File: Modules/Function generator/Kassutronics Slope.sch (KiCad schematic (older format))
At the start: 128 parts, among them J1 PJ301M-12, J10 Conn_01x08_Female, J11 Conn_01x08_Male, J12 Conn_01x05_Female, J13 Conn_01x05_Male, J14 Conn_01x06_Female, J15 Conn_01x06_Male, J2 PJ301M-12, J3 PJ301M-12, J4 PJ301M-12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

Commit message: Function generator: tweaked EOC and EOR circuits
Added diodes to gate outputs to prevent negative "low" value.
Also tweaked trigger thresholds based on simulations ( EOR comparator )
Added some additional comments to the schematic
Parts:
- removed C6, C7: 47p, Capacitor_SMD:C_0805_2012Metric_Pad1.15x1.40mm_HandSolder_smallText, symbol Device:C_Small
- removed D9: 1N5817, Diode_THT:D_DO-41_SOD81_P10.16mm_Horizontal, symbol Diode:1N5817
- added D20, D9: FDLL4148, Eurocad:LL4148_sam, symbol Diode:1N4148
- R26: value 1M -> 100k
- R32: value 100k -> 470k
- U3, U5: footprint (none) -> Package_SO:SOIC-14_3.9x8.7mm_P1.27mm
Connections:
- net EOC_out: now also D9.1 (K); no longer D11.2 (A), R32.1, U2.14
- net EOR_out: now also D20.1 (K); no longer U5.7
- net EORjack: now reaches J5.3, R42.1
- new net: D11.2 (A), D9.2 (A), R32.1, U2.14
- new net: D20.2 (A), U5.7
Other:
- note added: "At rest, STATE is low, so \npreceeding schmitt trigger\nis output low.\n\nWhen a trigger pulse comes in, \nassuming OUT is low, the schmitt\ntrigger turns on. \nNow the schmitt trigger's own output\nholds the +ve input high, even when \nthe trigger pulse has ended\n"
- note added: "Comparator"
- note added: "EOC comparator:\n( Schmitt trigger )\n\n\nEOC = TRUE if OUT < 120mV"
- note added: "STATE is high during the attack.\nMeanwhile OUT is rising.\nWhen OUT goes above 7.5V, the schmitt\ntrigger flips and then state goes negative"
- note added: "Sustain_buf = the voltage set by the pot if \nthe output of the Schmitt trigger is high\n( otherwise the sustain voltage is shorted to \nthe output of the schmitt trigger : near -12V )"
- note added: "To do:\n\nConsider moving D14 to lower PCB?\nCheck diode types\nGate output levels : Should we use zener diodes to give well-defined gate levels?"
- note removed: "EOC comparator:\n\nEOC = TRUE if OUT < 120mV"
- note removed: "STATE is high during the attack"
- note removed: "Sustain_buf = the voltage set by the pot if \nthe output of the Schmitt trigger is high\n( otherwise the sustain voltage is shorted to near -12 )"
- note removed: "To do:\n\nConsider moving D14 to lower PCB?\nCheck diode types\nGate output levels : needs a diode I think! Also a LM339 might give cleaner 0V / xV gates"
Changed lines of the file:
@@
 	9250 8000 9075 8000
 Connection ~ 10100 7900
-Text Notes 10475 7475 0    50   ~ 0
-STATE is high during the attack
+Text Notes 9075 6775 0    50   ~ 0
+STATE is high during the attack.\nMeanwhile OUT is rising.\nWhen OUT goes above 7.5V, the schmitt\ntrigger flips and then state goes negative
 Text GLabel 8425 9150 0    50   Input ~ 0
 OUT
 $Comp
-L Diode:1N5817 D9
-U 1 1 6080D78A
-P 8950 9375
-F 0 "D9" V 8904 9455 50  0000 L CNN
-F 1 "1N5817" V 8995 9455 50  0000 L CNN
-F 2 "Diode_THT:D_DO-41_SOD81_P10.16mm_Horizontal" H 8950 9200 50  0001 C CNN
-F 3 "http://www.vishay.com/docs/88525/1n5817.pdf" H 8950 9375 50  0001 C CNN
-	1    8950 9375
-	0    1    1    0
-$EndComp
-$Comp
 L Device:R R22
 U 1 1 6080F23B
@@
 	0    1    1    0
 $EndComp
-$Comp
-L power:GND #PWR018
-U 1 1 6080F96E
-P 8950 9625
-F 0 "#PWR018" H 8950 9375 50  0001 C CNN
-F 1 "GND" H 8955 9452 50  0000 C CNN
-F 2 "" H 8950 9625 50  0001 C CNN
-F 3 "" H 8950 9625 50  0001 C CNN
-	1    8950 9625
-	1    0    0    -1
-$EndComp
-Wire Wire Line
-	8950 9525 8950 9625
 Wire Wire Line
 	8425 9150 8550 9150
-Wire Wire Line
-	8850 9150 8950 9150
-Wire Wire Line
-	8950 9150 8950 9225
-Wire Wire Line
-	8950 9150 9075 9150
-Connection ~ 8950 9150
 Connection ~ 9075 9150
 $Comp
@@
 P 9625 8375
 F 0 "R26" V 9525 8375 50  0000 C CNN
-F 1 "1M" V 9625 8375 50  0000 C CNN
+F 1 "100k" V 9625 8375 50  0000 C CNN
 F 2 "Eurocad:R_0805_2012Metric_Pad1.15x1.40mm_HandSolder_smallText" V 9555 8375 50  0001 C CNN
 F 3 "~" H 9625 8375 50  0001 C CNN
@@
 P 10950 8475
 F 0 "R32" V 10850 8475 50  0000 C CNN
-F 1 "100k" V 10950 8475 50  0000 C CNN
+F 1 "470k" V 10950 8475 50  0000 C CNN
 F 2 "Eurocad:R_0805_2012Metric_Pad1.15x1.40mm_HandSolder_smallText" V 10880 8475 50  0001 C CNN
 F 3 "~" H 10950 8475 50  0001 C CNN
@@
 Wire Wire Line
 	12475 8075 11925 8075
-Text Notes 10450 9650 0    50   ~ 0
-EOC comparator:\n\nEOC = TRUE if OUT < 120mV
+Text Notes 10475 9825 0    50   ~ 0
+EOC comparator:\n( Schmitt trigger )\n\n\nEOC = TRUE if OUT < 120mV
 Text Notes 13375 7525 0    50   ~ 0
 EOR comparator\n\nEOR = NOT ( STATE, EOC )
@@
 	8825 12950 8825 13275
 Connection ~ 8825 13275
-$Comp
-L Device:C_Small C6
-U 1 1 608F4EDC
-P 9650 6900
-F 0 "C6" V 9421 6900 50  0000 C CNN
-F 1 "47p" V 9512 6900 50  0000 C CNN
-F 2 "Capacitor_SMD:C_0805_2012Metric_Pad1.15x1.40mm_HandSolder_smallText" H 9650 6900 50  0001 C CNN
-F 3 "~" H 9650 6900 50  0001 C CNN
-	1    9650 6900
-	0    1    1    0
-$EndComp
-Wire Wire Line
-	9750 6900 10100 6900
-Wire Wire Line
-	10100 6900 10100 7275
-Connection ~ 10100 7275
-Wire Wire Line
-	9550 6900 9050 6900
-Wire Wire Line
-	9050 6900 9050 7275
-Connection ~ 9050 7275
-$Comp
-L Device:C_Small C7
-U 1 1 609DCC24
-P 10950 8200
-F 0 "C7" V 10721 8200 50  0000 C CNN
-F 1 "47p" V 10812 8200 50  0000 C CNN
-F 2 "Capacitor_SMD:C_0805_2012Metric_Pad1.15x1.40mm_HandSolder_smallText" H 10950 8200 50  0001 C CNN
-F 3 "~" H 10950 8200 50  0001 C CNN
-	1    10950 8200
-	0    1    1    0
-$EndComp
-Wire Wire Line
-	11325 8475 11325 8200
-Wire Wire Line
-	11325 8200 11050 8200
-Wire Wire Line
-	10850 8200 10550 8200
-Wire Wire Line
-	10550 8200 10550 8475
-Connection ~ 10550 8475
 Wire Wire Line
 	9825 8950 10550 8950
@@
 	14975 7975 15625 7975
 Wire Wire Line
-	14950 9050 15550 9050
-Wire Wire Line
 	2575 11775 2575 10850
 Connection ~ 2575 10850
@@
 Wire Wire Line
 	6625 8175 6475 8175
-Text GLabel 15550 9000 1    50   Input ~ 0
-EOC_t
-Wire Wire Line
-	15550 9000 15550 9050
-Connection ~ 15550 9050
-Wire Wire Line
-	15550 9050 15650 9050
 Text GLabel 10300 7775 1    50   Input ~ 0
 STATE
@@
 	0    -1   -1   0
 $EndComp
-Text Notes 7425 5550 0    50   ~ 0
-Sustain_buf = the voltage set by the pot if \nthe output of the Schmitt trigger is high\n( otherwise the sustain voltage is shorted to near -12 )
+Text Notes 7400 5600 0    50   ~ 0
+Sustain_buf = the voltage set by the pot if \nthe output of the Schmitt trigger is high\n( otherwise the sustain voltage is shorted to \nthe output of the schmitt trigger : near -12V )
 Text Notes 4825 2450 0    50   ~ 0
 The integrator sees the highest of\n- the input\n- "state"\n- "sustain_buff"
@@
 Wire Wire Line
 	21225 10775 21225 10825
-Connection ~ 11325 9050
 Text GLabel 13925 9050 1    50   Input ~ 0
 EOC_out_t
@@
 Text GLabel 13850 13400 1    50   Input ~ 0
 SUSTAIN
-Wire Wire Line
-	11325 9050 13825 9050
-Wire Wire Line
-	13325 7975 13875 7975
 Text GLabel 19225 12075 1    50   Input ~ 0
 HOLD_INPUT_t
@@
 HOLD_INPUT
 Text Notes 700  1675 0    50   ~ 0
-To do:\n\nConsider moving D14 to lower PCB?\nCheck diode types\nGate output levels : needs a diode I think! Also a LM339 might give cleaner 0V / xV gates
+To do:\n\nConsider moving D14 to lower PCB?\nCheck diode types\nGate output levels : Should we use zener diodes to give well-defined gate levels?
 $Comp
 L power:GND #PWR0102
@@
 F 0 "U3" H 20633 3296 50  0000 L CNN
 F 1 "TL074" H 20633 3205 50  0000 L CNN
-F 2 "" H 20625 3350 50  0001 C CNN
+F 2 "Package_SO:SOIC-14_3.9x8.7mm_P1.27mm" H 20625 3350 50  0001 C CNN
 F 3 "http://www.ti.com/lit/ds/symlink/tl071.pdf" H 20725 3450 50  0001 C CNN
 	5    20675 3250
@@
 F 0 "U5" H 21658 3321 50  0000 L CNN
 F 1 "TL074" H 21658 3230 50  0000 L CNN
-F 2 "" H 21650 3375 50  0001 C CNN
+F 2 "Package_SO:SOIC-14_3.9x8.7mm_P1.27mm" H 21650 3375 50  0001 C CNN
 F 3 "http://www.ti.com/lit/ds/symlink/tl071.pdf" H 21750 3475 50  0001 C CNN
 	5    21700 3275
 	1    0    0    -1
 $EndComp
+$Comp
+L Diode:1N4148 D20
+U 1 1 61507C43
+P 13600 7975
+F 0 "D20" H 13600 7758 50  0000 C CNN
+F 1 "FDLL4148" H 13600 7849 50  0000 C CNN
+F 2 "Eurocad:LL4148_sam" H 13600 7800 50  0001 C CNN
+F 3 "https://assets.nexperia.com/documents/data-sheet/1N4148_1N4448.pdf" H 13600 7975 50  0001 C CNN
+	1    13600 7975
+	-1   0    0    1
+$EndComp
+Wire Wire Line
+	13875 7975 13750 7975
+Wire Wire Line
+	13450 7975 13325 7975
+$Comp
+L Diode:1N4148 D9
+U 1 1 61581F21
+P 11600 9050
+F 0 "D9" H 11600 8833 50  0000 C CNN
+F 1 "FDLL4148" H 11600 8924 50  0000 C CNN
+F 2 "Eurocad:LL4148_sam" H 11600 8875 50  0001 C CNN
+F 3 "https://assets.nexperia.com/documents/data-sheet/1N4148_1N4448.pdf" H 11600 9050 50  0001 C CNN
+	1    11600 9050
+	-1   0    0    1
+$EndComp
+Wire Wire Line
+	11450 9050 11325 9050
+Connection ~ 11325 9050
+Wire Wire Line
+	11750 9050 13825 9050
+Wire Wire Line
+	8850 9150 9075 9150
+Text Notes 9575 8075 0    50   ~ 0
+Schmitt trigger
+Text Notes 13025 8150 0    50   ~ 0
+Comparator
+Text Notes 7525 7225 0    50   ~ 0
+At rest, STATE is low, so \npreceeding schmitt trigger\nis output low.\n\nWhen a trigger pulse comes in, \nassuming OUT is low, the schmitt\ntrigger turns on. \nNow the schmitt trigger's own output\nholds the +ve input high, even when \nthe trigger pulse has ended\n
+Wire Wire Line
+	14950 9050 15650 9050
+Text Label 15525 7975 1    50   ~ 0
+EORjack
+Text GLabel 15375 9050 1    50   Input ~ 0
+EOC_t
 $EndSCHEMATC

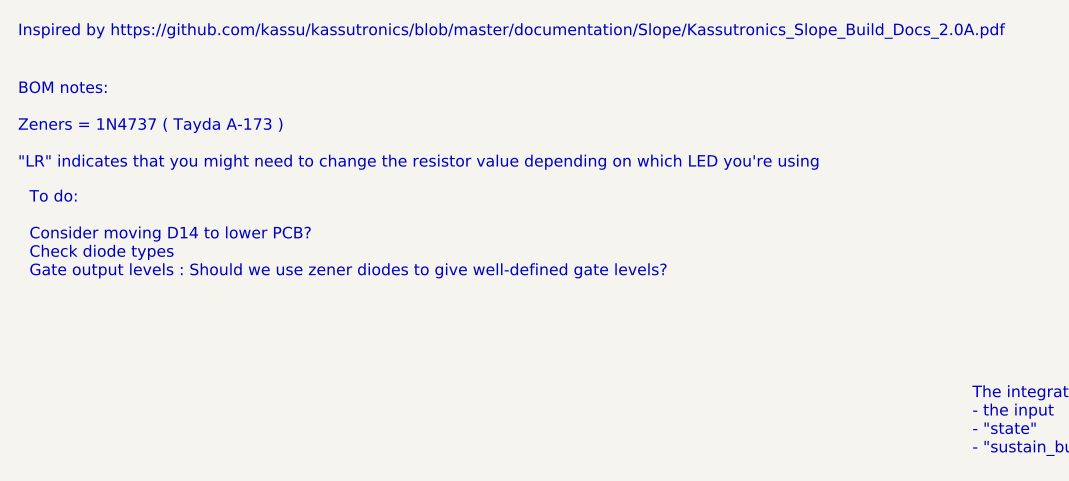
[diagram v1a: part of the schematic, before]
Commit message: Board tweaks
- Changed to zeners with smaller footprint
- Added board markings
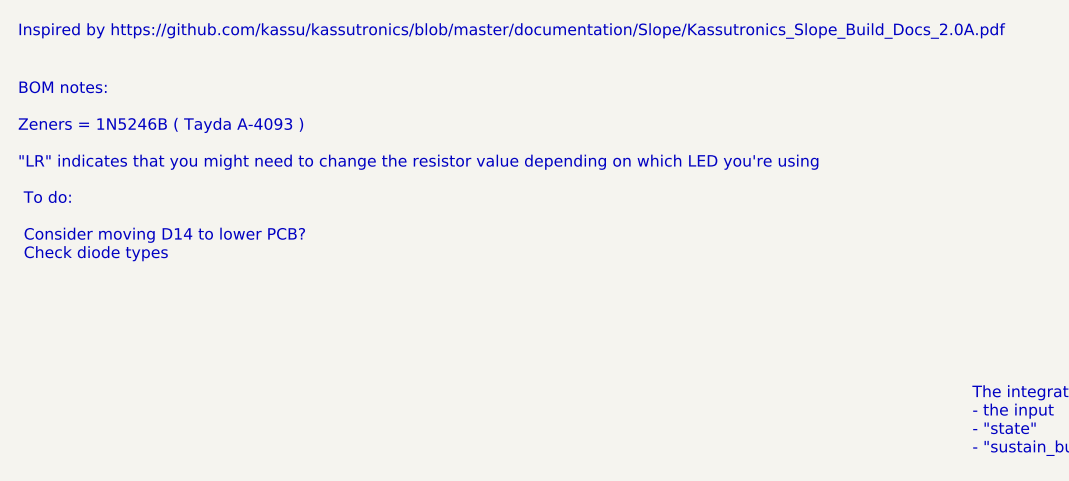
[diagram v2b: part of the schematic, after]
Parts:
- D19, D5, D6, D8: footprint Diode_THT:D_DO-41_SOD81_P7.62mm_Horizontal -> Diode_THT:D_DO-35_SOD27_P7.62mm_Horizontal
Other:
- note added: "BOM notes:\n \nZeners = 1N5246B ( Tayda A-4093 ) \n\n"LR" indicates that you might need to change the resistor value depending on which LED you're using\n"
- note added: "To do:\n\nConsider moving D14 to lower PCB?\nCheck diode types"
- note removed: "BOM notes:\n \nZeners = 1N4737 ( Tayda A-173 )\n\n"LR" indicates that you might need to change the resistor value depending on which LED you're using\n"
- note removed: "To do:\n\nConsider moving D14 to lower PCB?\nCheck diode types\nGate output levels : Should we use zener diodes to give well-defined gate levels?"
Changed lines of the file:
@@
 F 0 "D5" V 7704 3780 50  0000 L CNN
 F 1 "7.5V" V 7795 3780 50  0000 L CNN
-F 2 "Diode_THT:D_DO-41_SOD81_P7.62mm_Horizontal" H 7750 3700 50  0001 C CNN
+F 2 "Diode_THT:D_DO-35_SOD27_P7.62mm_Horizontal" H 7750 3700 50  0001 C CNN
 F 3 "~" H 7750 3700 50  0001 C CNN
 	1    7750 3700
@@
 F 0 "D6" V 7796 4070 50  0000 R CNN
 F 1 "7.5V" V 7705 4070 50  0000 R CNN
-F 2 "Diode_THT:D_DO-41_SOD81_P7.62mm_Horizontal" H 7750 4150 50  0001 C CNN
+F 2 "Diode_THT:D_DO-35_SOD27_P7.62mm_Horizontal" H 7750 4150 50  0001 C CNN
 F 3 "~" H 7750 4150 50  0001 C CNN
 	1    7750 4150
@@
 F 0 "D8" V 8579 8180 50  0000 L CNN
 F 1 "7.5V" V 8670 8180 50  0000 L CNN
-F 2 "Diode_THT:D_DO-41_SOD81_P7.62mm_Horizontal" H 8625 8100 50  0001 C CNN
+F 2 "Diode_THT:D_DO-35_SOD27_P7.62mm_Horizontal" H 8625 8100 50  0001 C CNN
 F 3 "~" H 8625 8100 50  0001 C CNN
 	1    8625 8100
@@
 F 0 "D19" V 22479 2280 50  0000 L CNN
 F 1 "7.5V" V 22570 2280 50  0000 L CNN
-F 2 "Diode_THT:D_DO-41_SOD81_P7.62mm_Horizontal" H 22525 2200 50  0001 C CNN
+F 2 "Diode_THT:D_DO-35_SOD27_P7.62mm_Horizontal" H 22525 2200 50  0001 C CNN
 F 3 "~" H 22525 2200 50  0001 C CNN
 	1    22525 2200
@@
 Connection ~ 21225 10825
 Text Notes 650  1200 0    50   ~ 0
-BOM notes:\n \nZeners = 1N4737 ( Tayda A-173 )\n\n"LR" indicates that you might need to change the resistor value depending on which LED you're using\n
+BOM notes:\n \nZeners = 1N5246B ( Tayda A-4093 ) \n\n"LR" indicates that you might need to change the resistor value depending on which LED you're using\n
 Wire Wire Line
 	2300 12575 2325 12575
@@
 Text GLabel 13950 13400 1    50   Input ~ 0
 HOLD_INPUT
-Text Notes 700  1675 0    50   ~ 0
-To do:\n\nConsider moving D14 to lower PCB?\nCheck diode types\nGate output levels : Should we use zener diodes to give well-defined gate levels?
+Text Notes 675  1600 0    50   ~ 0
+To do:\n\nConsider moving D14 to lower PCB?\nCheck diode types
 $Comp
 L power:GND #PWR0102

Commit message: Updated readme
Updated readme with status of the various projects

Also added photos/renders of the boards for the various projects

There's also some other additions which are autogenerated by KiCad - don't worry about them...
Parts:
- added R55, R56: 470k, Eurocad:R_0805_2012Metric_Pad1.15x1.40mm_HandSolder_smallText, symbol Device:R
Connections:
- net EOC_out_t: now also R56.1
- net EOR_out_t: now also R55.1
- net GND: now also R55.2, R56.2
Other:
- note added: "Original schematic uses TLC3702 comparators \n(push-pull ) to drive the EOR and EOC outputs. \nTayda only has 339 type ( open collector )\n\nI'm just going to use a TL07x as comparator,\neven though I guess it's sub-optimal\n\nThe 470k resistors ensure that current flows through\nthe diode ( and therefore the "off" voltage is 0v ) \neven if the output it plugged into something with\ninfinitely hi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"
- note removed: "Original schematic uses TLC3702 comparators \n(push-pull ) to drive the EOR and EOC outputs. \nTayda only has 339 type ( open collector )\n\nI'm just going to use a TL07x as comparator,\neven though I guess it's sub-optimal"
- moved on the sheet: R41, R42
